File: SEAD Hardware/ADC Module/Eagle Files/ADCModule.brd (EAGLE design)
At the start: 79.9 x 48.9 mm, 66 parts, among them U1 ADS8568_PM_64, U2 LP2950-3.3ACZ, U6 TPS7A3301_RGW_20

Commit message: More compute unit work.
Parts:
- removed C1, C2, C3, C4, C46, C47, C48, C5, C53, C54, C56, C6, C7: 10uF, SensorCape:0805
- removed C18, C28, C30, C58: 1uF, SensorCape:0805
- removed C19, C34: 10uF, SensorCape:1206
- removed C20, C21, C22, C23, C24, C25, C26, C27, C29, C32: 10uF, ASL:0805
- removed C31: 10nF, SensorCape:0805
- removed C33: 10uF, SensorCape:CPOL-RADIAL-10UF-25V
- removed C55, C57, C59, C60, C61, C62, C64, C71: .1uF, SensorCape:0805
- removed C63: .47uF, SensorCape:0805
- removed JP1, JP2: M03-SCREW-5MM, ASL:SCREWTERMINAL-5MM-3
- removed R23: 1.5M, ASL:0805
- removed R24: 162k, ASL:0805
- removed SL1: (no value), ASL:1X04_LOCK
- removed U$2, U$3: TPS7A4700_RGW_20, SensorCape:RGW20_3P15X3P15
- removed U1: ADS8568_PM_64, SensorCape:PM64
- removed U2: LP2950-3.3ACZ, ASL:TO92
- removed U6: TPS7A3301_RGW_20, SensorCape:RGW20_3P15X3P15
- added X1: 52885-0374, SensorCape:52885-0374
- C8: device SensorCape:1206 -> SensorCape:0805
- moved JP6 47.6 mm to (26.7, 1.52), turned to 0 degrees
- moved C13 43.1 mm to (28.3, 35.2)
- moved C9 42.3 mm to (31.1, 35.1), turned to 270 degrees
- moved C12 41.8 mm to (29.6, 16.2), turned to 90 degrees
- moved C10 40.1 mm to (18.1, 25.7), turned to 0 degrees
- moved C11 39.2 mm to (23.5, 16.1)
- moved R2 37.7 mm to (24.6, 4.64), turned to 180 degrees
- moved C8 35.0 mm to (18.1, 27.2), turned to 0 degrees
- moved C17 34.5 mm to (24.6, 6.25)
- moved LED1 33.2 mm to (36.3, 18.9)
- moved U$1 33.1 mm to (27.9, 25.5)
- moved R1 32.7 mm to (27.6, 4.63), turned to 0 degrees
- moved R3 32.2 mm to (38.0, 18.9), turned to 90 degrees
- moved C16 29.4 mm to (37.0, 21.8), turned to 180 degrees
- moved C14 24.4 mm to (37.2, 29.2), turned to 180 degrees
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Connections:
- removed net A0: JP1.3, U1.42
- removed net A1: JP1.2, U1.47
- removed net B0: JP1.1, U1.49
- removed net B1: JP2.3, U1.54
- removed net BUSY: U$1.47, U1.35
- removed net C0: JP2.2, U1.64
- removed net C1: JP2.1, U1.59
- removed net CONV_A: U$1.44, U1.37
- removed net CONV_B: U$1.43, U1.38
- removed net CONV_C: U1.39
- removed net CONV_D: U1.40
- removed net CS*: U$1.40, U1.13
- removed net D0: U1.7
- removed net D1: U1.2
- removed net HVDD_12A: C20.1, C21.1, C22.1, C23.1, C24.1, C56.2, C57.2, C6.1, C7.1, U$2.1, U$2.20, U$2.3, U$3.13, U$3.15, U$3.16, U1.48, U2.3
- removed net HVDD_15D: C19.1, U$2.13, U$2.15, U$2.16
- removed net HVSS_12A: C25.1, C26.1, C27.1, C29.1, C31.1, C32.1, C54.2, C55.2, R23.2, U1.1, U6.1, U6.20
- removed net HVSS_15D: C34.2, U6.13, U6.15, U6.16
- removed net N$33: C30.1, U6.14
- removed net N$45: C28.1, U$3.14
- removed net N$6: C18.1, U$2.14
- removed net N$7: C63.1, U1.56
- removed net N$8: C31.2, R23.1, R24.2, U6.3
- removed net N$87: C46.2, U1.6
- removed net N$93: C53.2, U1.43
- removed net N$94: C48.2, U1.50
- removed net N$96: C47.1, U1.63
- removed net PMP1: U$1.82, U1.32
- removed net PMP10: U$1.95, U1.21
- removed net PMP11: U$1.96, U1.20
- removed net PMP12: U$1.97, U1.19
- removed net PMP13: U$1.98, U1.18
- removed net PMP14: U$1.99, U1.17
- removed net PMP15: U$1.100, U1.16
- removed net PMP2: U$1.87, U1.31
- removed net PMP3: U$1.88, U1.30
- removed net PMP4: U$1.89, U1.29
- removed net PMP5: U$1.90, U1.28
- removed net PMP6: U$1.91, U1.27
- removed net PMP7: U$1.92, U1.26
- removed net PMP8: U$1.93, U1.23
- removed net PMP9: U$1.94, U1.22
- removed net RD*: U$1.41, U1.12
- removed net RX1A: U$1.52
- removed net TX1A: U$1.53
- removed net VDD5V0_A: C1.1, C2.1, C3.1, C4.1, C5.1, C59.1, C60.1, C61.2, C62.2, C64.1, C71.1, U$3.1, U$3.20, U$3.3, U1.14, U1.4, U1.45, U1.52, U1.57, U1.61
- removed net WR*: U$1.42, U1.11
- new net CANRX: U$1.87
- new net CANTX: U$1.88
- new net N$1: U$1.63
- new net N$2: U$1.64
- new net SCL: U$1.58, X1.16
- new net SDA: U$1.59, X1.14
- new net U1RX: U$1.52, X1.22
- new net U1TX: U$1.53, X1.20
- new net U3RX: U$1.49, X1.28
- new net U3TX: U$1.50, X1.26
- net GND: now also X1.1, X1.12, X1.18, X1.2, X1.24, X1.29, X1.30; no longer C1.2, C18.2, C19.2, C2.2, C20.2, C21.2, C22.2, C23.2, C24.2, C25.2, C26.2, C27.2, C28.2, C29.2, C3.2, C30.2, C32.2, C33.2, C34.1, C4.2, C46.1, C47.2, C48.1, C5.2, C53.1, C54.1, C55.1, C56.1, C57.1, C58.1, C59.2, C6.2, C60.2, C61.1, C62.1, C63.2, C64.2, C7.2, C71.2, R24.1, U$2.11, U$2.21, U$2.4, U$2.6, U$2.7, U$2.9, U$3.10, U$3.21, U$3.6, U$3.7, U1.10, U1.15, U1.24, U1.3, U1.34, U1.36, U1.44, U1.46, U1.5, U1.51, U1.53, U1.55, U1.58, U1.60, U1.62, U1.8, U2.2, U6.21, U6.7
- net MISO: now also X1.4; no longer SL1.2
- net MOSI: now also X1.6; no longer SL1.3
- net PMP0: no longer U1.33
- net SCK: now also X1.10; no longer SL1.1
- net SS: now also X1.8; no longer SL1.4
- net VDD3V3_D: no longer C33.1, C58.2, U1.25, U1.41, U1.9, U2.1
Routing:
- net VDD3V3_D: track 226.2 -> 16.8 mm, vias 9 -> 0
- net HVDD_12A: track 115.1 -> 0.00 mm, vias 2 -> 0
- net VDD5V0_A: track 110.2 -> 0.00 mm, vias 3 -> 0
- net WR*: track 86.4 -> 0.00 mm
- net RD*: track 82.9 -> 0.00 mm
- net CS*: track 78.9 -> 0.00 mm
- net CONV_B: track 69.5 -> 0.00 mm
- net GND: track 79.1 -> 12.8 mm, vias 81 -> 0
- net CONV_A: track 66.0 -> 0.00 mm
- net B0: track 59.7 -> 0.00 mm, vias 2 -> 0
- net BUSY: track 54.1 -> 0.00 mm
- net A1: track 46.3 -> 0.00 mm, vias 1 -> 0
- net HVSS_12A: track 45.6 -> 0.00 mm, vias 2 -> 0
- net A0: track 43.2 -> 0.00 mm
- net C0: track 37.1 -> 0.00 mm, vias 3 -> 0
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- removed copper zone on layer 1, net HVDD_12A
- removed copper zone on layer 1, net HVDD_15D
- removed copper zone on layer 1, net HVSS_15D
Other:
- board size 79.9 x 48.9 mm -> 44.9 x 48.9 mm
- board text removed: "MISO"
- board text removed: "MOSI"
- board text removed: "SCK"
- board text removed: "SS"
- board text removed: "URX"
- board text removed: "UTX"

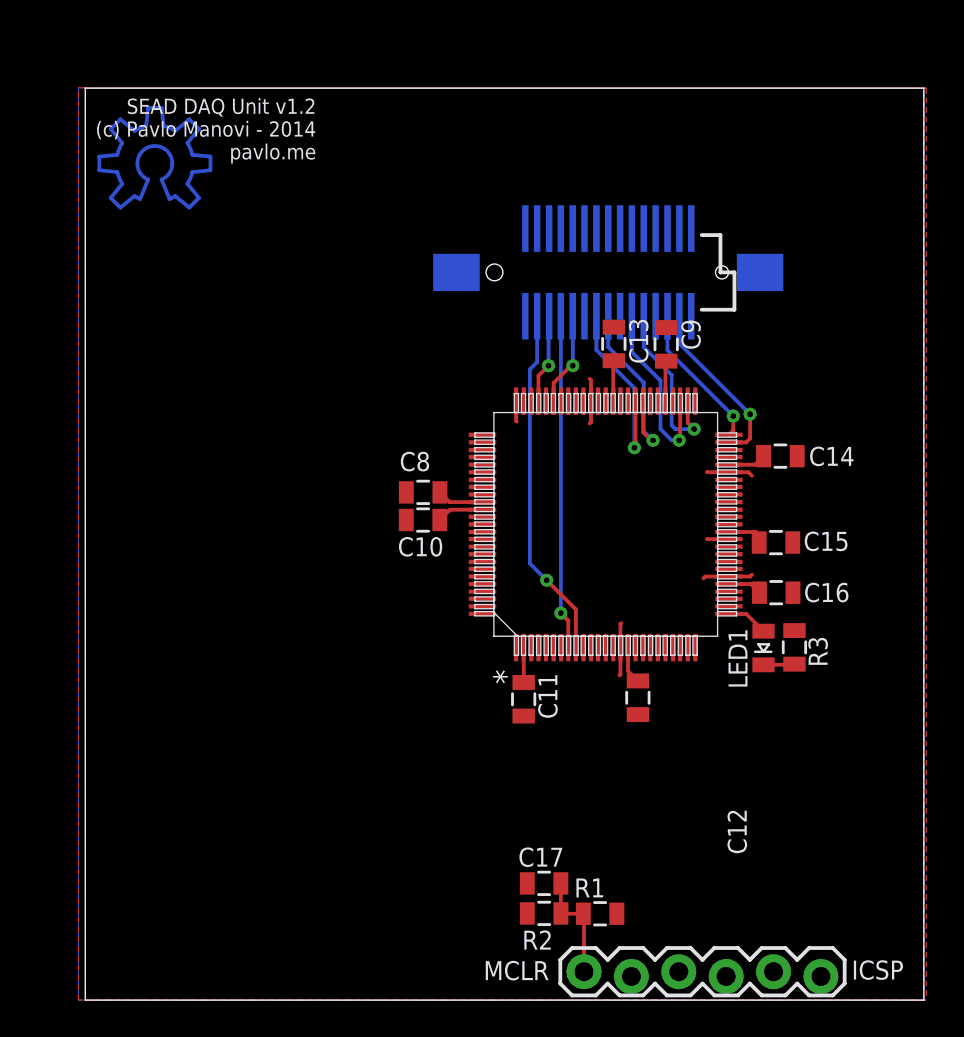
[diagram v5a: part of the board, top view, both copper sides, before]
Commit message: Compute module clock sources.
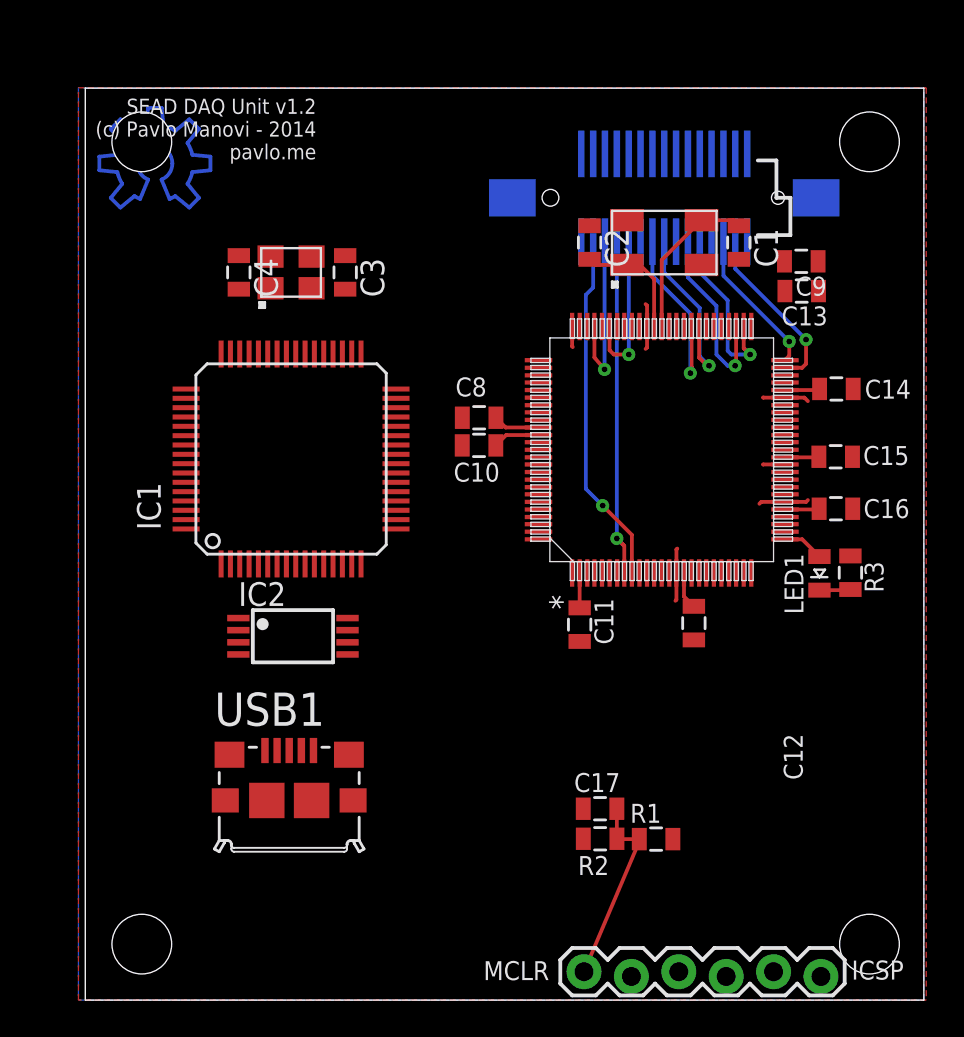
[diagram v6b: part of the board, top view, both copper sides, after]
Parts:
- added C1, C2: 36pF, SensorCape:0805
- added C3, C4: 20pF, SensorCape:0805
- added IC1: (no value), SensorCape:LQFP64
- added IC2: 93-C46AST, microchip:TSSOP8
- added U$2: ABM3B-8.000MHZ-10-1-U-T, SensorCape:ABM3B
- added U$3: 7M-12.000MEEQ-T, SensorCape:7M-CRYSTAL
- added USB1: CON-USB-F-MICRO-B, dp_devices.v6:CONN_USB_MICRO-B
- moved C13 10.5 mm to (38.4, 38.0), turned to 180 degrees
- moved C9 8.50 mm to (38.3, 39.6), turned to 180 degrees
- moved C15 5.60 mm to (40.2, 29.1)
- moved C16 5.52 mm to (40.2, 26.3)
- moved C17 5.00 mm to (27.6, 10.3)
- moved C10 5.00 mm to (21.1, 29.7)
- moved C11 5.00 mm to (26.5, 20.1)
- moved C12 5.00 mm to (32.6, 20.2)
- moved C8 5.00 mm to (21.1, 31.2)
- moved LED1 5.00 mm to (39.3, 22.9)
- moved R1 5.00 mm to (30.6, 8.63)
- moved R2 5.00 mm to (27.6, 8.64)
- moved R3 5.00 mm to (41.0, 22.9)
- moved U$1 5.00 mm to (30.9, 29.5)
- moved X1 5.00 mm to (31.0, 43.0)
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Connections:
- new net N$10: IC1.7, USB1.P2
- new net N$11: IC1.8, USB1.P3
- new net N$8: C3.1, U$3.3
- new net N$9: C4.2, U$3.1
- new net VCC: IC2.8
- net GND: now also C1.2, C2.1, C3.2, C4.1, IC2.5, U$2.2, U$2.4, U$3.2, U$3.4
- net N$1: now also C1.1, U$2.3
- net N$2: now also C2.2, U$2.1
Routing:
- net N$1: track 0.00 -> 8.99 mm
- net N$2: track 0.00 -> 6.52 mm
- net VDD3V3_D: track 16.8 -> 12.0 mm
- net MCLR: track 5.94 -> 10.6 mm
- net MOSI: track 4.79 -> 9.36 mm
- net SCK: track 5.04 -> 8.45 mm

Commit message: Layout work.
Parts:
- added C18: 2.2uF, SensorCape:0805
- added C19: 4.7uF, SensorCape:0805
- added C20: 3.3uF, SensorCape:EIA3216
- added C21, C22: 4.7uF, SensorCape:EIA3216
- added C23, C24, C5: .1uF, SensorCape:0805
- added C6: 100uF, SensorCape:1206
- added C7: .01uF, SensorCape:0805
- added L1, L2: (no value), dp_devices.v6:FB805
- added LED2, LED3: (no value), led:CHIP-LED0805
- added R10, R11: 470, SensorCape:0805
- added R4, R5, R6, R8: 10k, SensorCape:0805
- added R7: 2.2k, SensorCape:0805
- added R9: 12k 1%, SensorCape:0805
- added U1: LP2989_DGK_8, SensorCape:MUA08A
- C1, C2: value 36pF -> 20pF
- R3: value (none) -> 330
- moved C3 28.0 mm to (-10.7, 25.6), turned to 0 degrees
- moved U$3 27.1 mm to (-10.7, 22.7), turned to 90 degrees
- moved C4 26.9 mm to (-10.7, 19.9), turned to 0 degrees
- moved IC2 14.6 mm to (3.00, 31.6), turned to 0 degrees
- moved USB1 8.06 mm to (11.9, 2.70)
- moved C8 2.30 mm to (20.0, 29.2), turned to 90 degrees
- moved IC1 1.41 mm to (12.0, 30.0)
- moved C10 0.82 mm to (21.7, 29.2), turned to 90 degrees
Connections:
- removed net PMP0: U$1.80
- removed net VCC: IC2.8
- new net A0: IC1.27, U$1.44
- new net CS*: IC1.26, U$1.71
- new net D0: IC1.16, U$1.93
- new net D1: IC1.17, U$1.94
- new net D2: IC1.18, U$1.98
- new net D3: IC1.19, U$1.99
- new net D4: IC1.21, U$1.100
- new net D5: IC1.22, U$1.3
- new net D6: IC1.23, U$1.4
- new net D7: IC1.24, U$1.5
- new net N$12: IC1.63, IC2.1, R4.1
- new net N$13: IC1.62, IC2.2, R5.1
- new net N$17: IC2.4, R6.1, R7.1
- new net N$18: IC1.61, IC2.3, R7.2
- new net N$19: IC1.14, R8.1
- new net N$20: IC1.6, R9.1
- new net N$21: C22.A, C24.1, IC1.4, L2.1
- new net N$22: C21.A, C23.1, IC1.9, L1.1
- new net N$23: C7.2, U1.1
- new net N$24: C18.2, C7.1, U1.3
- new net N$27: IC1.48
- new net N$28: IC1.54, R10.2
- new net N$29: IC1.55, R11.2
- new net N$32: LED2.C, R10.1
- new net N$33: LED3.C, R11.1
- new net RD*: IC1.28, U$1.82
- new net SIWUA: IC1.30
- new net USB_UART_RX: IC1.39, U$1.12
- new net USB_UART_TX: IC1.38, U$1.11
- new net VDD1V8_D: C20.A, IC1.12, IC1.37, IC1.49, IC1.64
- new net VDD5V0_D: C18.1, C6.2, U1.4, U1.8, USB1.P1, X1.3
- new net WR*: IC1.29, U$1.81
- net CANRX: now also X1.7
- net CANTX: now also X1.9
- net GND: now also C19.1, C20.C, C21.C, C22.C, C23.2, C24.2, C5.2, C6.1, IC1.1, IC1.10, IC1.11, IC1.13, IC1.15, IC1.25, IC1.35, IC1.47, IC1.5, IC1.51, R9.2, USB1.P5
- net N$8: now also IC1.3
- net N$9: now also IC1.2
- net VDD3V3_D: now also C19.2, C5.1, IC1.20, IC1.31, IC1.42, IC1.50, IC1.56, IC2.8, L1.2, L2.2, LED2.A, LED3.A, R4.2, R5.2, R6.2, R8.2, U1.5, U1.6, X1.5
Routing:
- net USB_UART_RX: track 0.00 -> 31.3 mm, vias 0 -> 2
- net USB_UART_TX: track 0.00 -> 28.7 mm, vias 0 -> 2
- net D7: track 0.00 -> 20.5 mm, vias 0 -> 2
- net D6: track 0.00 -> 18.9 mm, vias 0 -> 2
- net D5: track 0.00 -> 17.4 mm, vias 0 -> 2
- net GND: track 12.8 -> 26.8 mm
- net D4: track 0.00 -> 12.6 mm
- net D3: track 0.00 -> 10.8 mm
- net D1: track 0.00 -> 7.28 mm, vias 0 -> 2
- net D2: track 0.00 -> 7.15 mm
- net RD*: track 0.00 -> 6.69 mm
- net WR*: track 0.00 -> 6.65 mm
- net N$4: track 2.50 -> 5.06 mm

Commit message: More board layout work.
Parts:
- moved C20 37.8 mm to (6.30, 43.4), turned to 270 degrees
- moved C19 25.1 mm to (19.1, 17.3)
- moved C4 17.2 mm to (2.50, 30.9), turned to 180 degrees
- moved U$3 14.4 mm to (2.60, 28.1), turned to 270 degrees
- moved C22 14.0 mm to (8.40, 26.2), turned to 0 degrees
- moved C3 13.2 mm to (2.50, 25.3), turned to 180 degrees
- moved LED3 12.4 mm to (13.9, 46.4), turned to 90 degrees
- moved R7 12.2 mm to (2.50, 37.2), turned to 180 degrees
- moved R9 11.9 mm to (5.90, 29.5)
- moved R11 11.3 mm to (10.6, 46.4), turned to 180 degrees
- moved C5 11.0 mm to (2.50, 47.3)
- moved IC2 10.9 mm to (2.50, 42.5)
- moved L2 10.2 mm to (8.90, 22.6), turned to 180 degrees
- moved LED2 10.1 mm to (13.9, 44.9), turned to 90 degrees
- moved C24 10.0 mm to (8.90, 24.2), turned to 180 degrees
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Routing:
- net N$12: track 0.00 -> 28.6 mm, vias 0 -> 2
- net N$11: track 0.00 -> 25.1 mm
- net N$10: track 0.00 -> 25.0 mm
- net N$13: track 0.00 -> 23.5 mm, vias 0 -> 2
- net VDD1V8_D: track 0.00 -> 22.2 mm
- net N$18: track 0.00 -> 18.4 mm, vias 0 -> 2
- net N$29: track 0.00 -> 17.4 mm
- net N$28: track 0.00 -> 15.5 mm
- net USB_UART_RX: track 31.3 -> 19.3 mm
- net N$9: track 0.00 -> 11.2 mm
- net USB_UART_TX: track 28.7 -> 18.7 mm
- net N$8: track 0.00 -> 9.91 mm
- net D7: track 20.5 -> 11.5 mm
- net N$22: track 0.00 -> 8.33 mm
- net D6: track 18.9 -> 11.0 mm
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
